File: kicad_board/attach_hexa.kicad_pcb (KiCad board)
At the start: 2 copper layers, 91.3 x 25.9 mm, 26 parts, among them J1 Conn_01x15_Male, J2 TACH, J3 Conn_01x15, J4 Conn_01x15, J5 Conn_01x15_Male, Q1 2N3904, Q2 2N3904, Q3 2N3904, Q4 2N3904, Q5 2N3904, Q6 2N3904

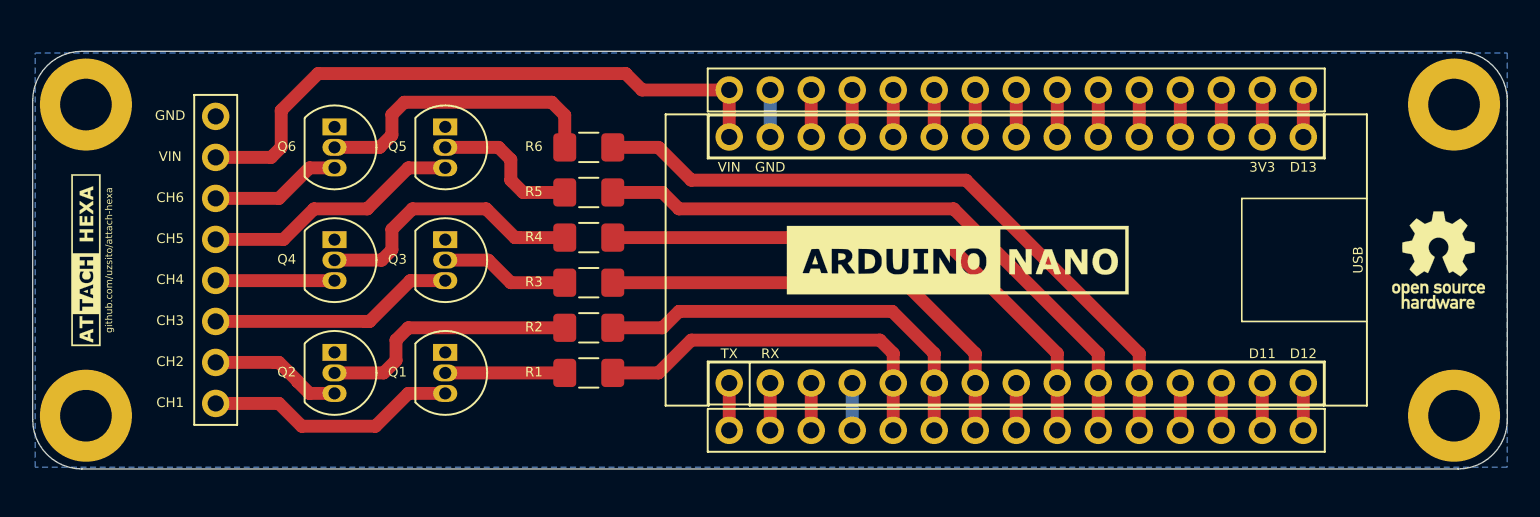
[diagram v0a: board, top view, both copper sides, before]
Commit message: Changed SMD sizes to ease hand soldering. Improved silkscreen visibility.
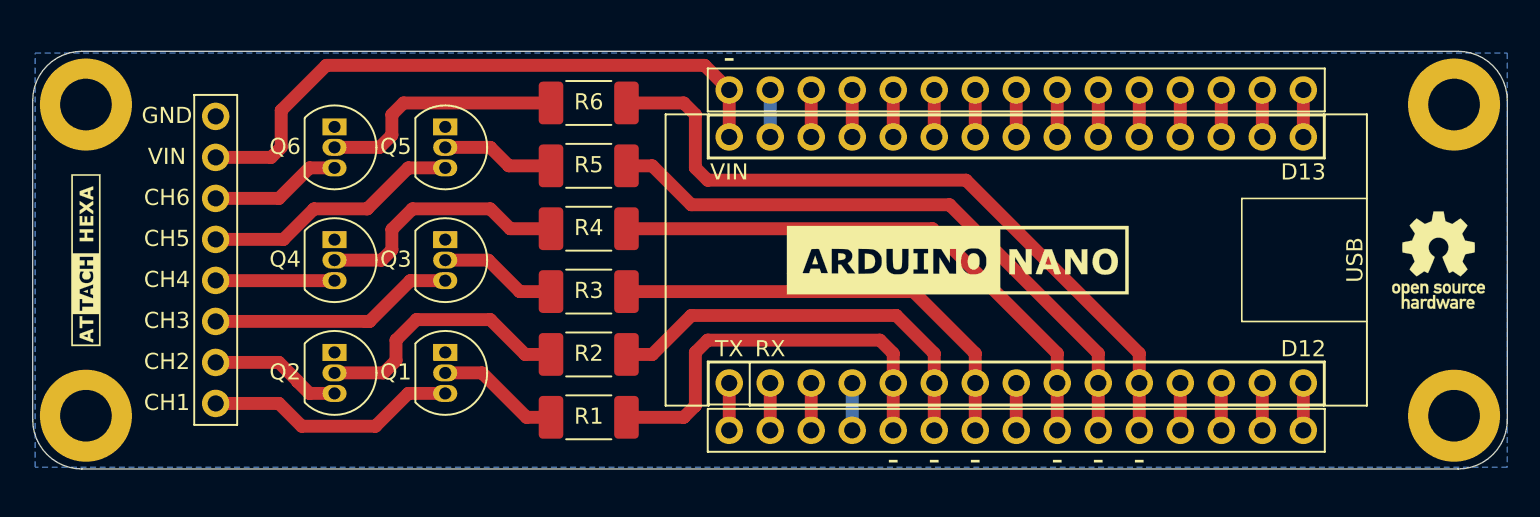
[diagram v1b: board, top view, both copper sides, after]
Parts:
- R1, R2, R3, R4, R5, R6: footprint Resistor_SMD:R_1206_3216Metric_Pad1.42x1.75mm_HandSolder -> Resistor_SMD:R_2010_5025Metric_Pad1.52x2.65mm_HandSolder
- moved R1 2.75 mm to (166.9, 87.8)
- moved R6 2.75 mm to (166.9, 68.4)
- moved R5 1.65 mm to (166.9, 72.3)
- moved R2 1.65 mm to (166.9, 83.9)
- moved R3 0.55 mm to (166.9, 80.1)
- moved R4 0.55 mm to (166.9, 76.2)
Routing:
- net Net-(Q6-Pad2): track 18.5 -> 15.3 mm
- net Net-(Q5-Pad2): track 9.30 -> 7.03 mm
- net Net-(A1-Pad5): track 23.3 -> 25.5 mm
- net Net-(A1-Pad11): track 42.7 -> 44.9 mm
- net Net-(A1-Pad7): track 29.0 -> 28.0 mm
- net Net-(Q4-Pad2): track 17.1 -> 16.0 mm
- net Net-(A1-Pad9): track 35.3 -> 34.6 mm
- net Net-(Q3-Pad2): track 7.98 -> 7.36 mm
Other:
- board text added: "-"
- board text removed: "github.com/uzsito/attach-hexa"

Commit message: Minor trace routing, positioning and silkscreen adjustments
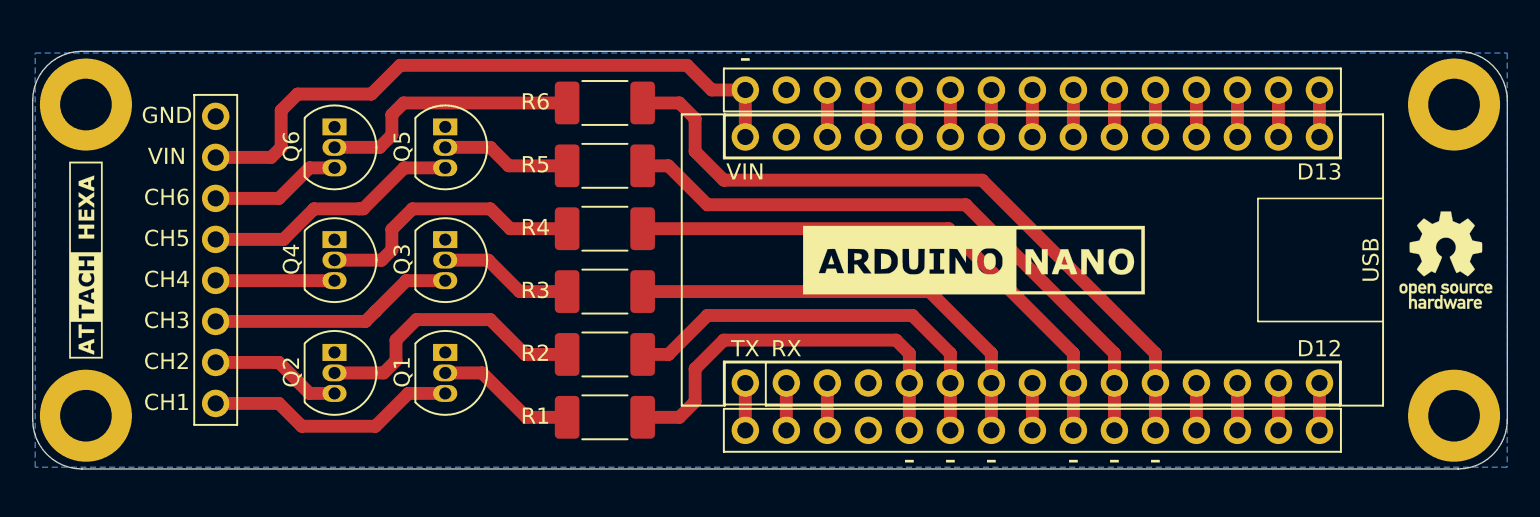
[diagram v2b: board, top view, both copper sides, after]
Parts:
- removed the G*** at (135.7, 78.1)
- added G***: LOGO, Symbol:attach_hexa_logo2, F.Cu at (135.7, 78.1)
- moved A1 1.00 mm to (176.6, 85.7)
- moved G*** 1.00 mm to (190.7, 78.1)
- moved J1 1.00 mm to (212.1, 67.6)
- moved J3 1.00 mm to (212.1, 70.5)
- moved J4 1.00 mm to (176.6, 85.7)
- moved J5 1.00 mm to (176.6, 88.6)
- moved R1 1.00 mm to (167.9, 87.8)
- moved R2 1.00 mm to (167.9, 83.9)
- moved R3 1.00 mm to (167.9, 80.1)
- moved R4 1.00 mm to (167.9, 76.2)
- moved R5 1.00 mm to (167.9, 72.3)
- moved R6 1.00 mm to (167.9, 68.4)
- moved REF** 0.45 mm to (220.0, 78.1)
- moved REF** 0.24 mm to (194.4, 77.3)
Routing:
- net GND: track 5.84 -> 0.00 mm
- net Net-(A1-Pad30): track 38.5 -> 39.5 mm
- net Net-(Q6-Pad2): track 15.3 -> 16.3 mm
- net Net-(Q5-Pad2): track 7.03 -> 8.03 mm
- net Net-(Q4-Pad2): track 16.0 -> 17.0 mm
- net Net-(Q3-Pad2): track 7.36 -> 8.36 mm
- net Net-(Q2-Pad2): track 16.4 -> 17.4 mm
- net Net-(Q1-Pad2): track 7.69 -> 8.69 mm
- net Net-(A1-Pad11): track 44.9 -> 44.1 mm
- net Net-(A1-Pad5): track 25.5 -> 24.8 mm

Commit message: Set base resistors to 4.7k - force transistor saturation up to 10mA collector current
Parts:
- R1, R2, R3, R4, R5, R6: value R -> 4,7k
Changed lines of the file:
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@@
   )
   (setup
-    (last_trace_width 0.8)
+    (last_trace_width 0.25)
     (user_trace_width 0.6)
     (user_trace_width 0.8)
@@
       (effects (font (size 1 1) (thickness 0.15)))
     )
-    (fp_text value R (at 0 2.28) (layer F.Fab)
+    (fp_text value 4,7k (at 0 2.28) (layer F.Fab)
       (effects (font (size 1 1) (thickness 0.15)))
     )
@@
       (effects (font (size 1 1) (thickness 0.15)))
     )
-    (fp_text value R (at 0 2.28) (layer F.Fab)
+    (fp_text value 4,7k (at 0 2.28) (layer F.Fab)
       (effects (font (size 1 1) (thickness 0.15)))
     )
@@
       (effects (font (size 1 1) (thickness 0.15)))
     )
-    (fp_text value R (at 0 2.28) (layer F.Fab)
+    (fp_text value 4,7k (at 0 2.28) (layer F.Fab)
       (effects (font (size 1 1) (thickness 0.15)))
     )
@@
       (effects (font (size 1 1) (thickness 0.15)))
     )
-    (fp_text value R (at 0 2.28) (layer F.Fab)
+    (fp_text value 4,7k (at 0 2.28) (layer F.Fab)
       (effects (font (size 1 1) (thickness 0.15)))
     )
@@
       (effects (font (size 1 1) (thickness 0.15)))
     )
-    (fp_text value R (at 0 2.28) (layer F.Fab)
+    (fp_text value 4,7k (at 0 2.28) (layer F.Fab)
       (effects (font (size 1 1) (thickness 0.15)))
     )
@@
       (effects (font (size 1 1) (thickness 0.15)))
     )
-    (fp_text value R (at 0 2.28) (layer F.Fab)
-      (effects (font (size 1 1) (thickness 0.15)))
-    )
+    (fp_text value 4,7k (at 0 2.28) (layer F.Fab)
+      (effects (font (size 1 1) (thickness 0.15)))
+    )

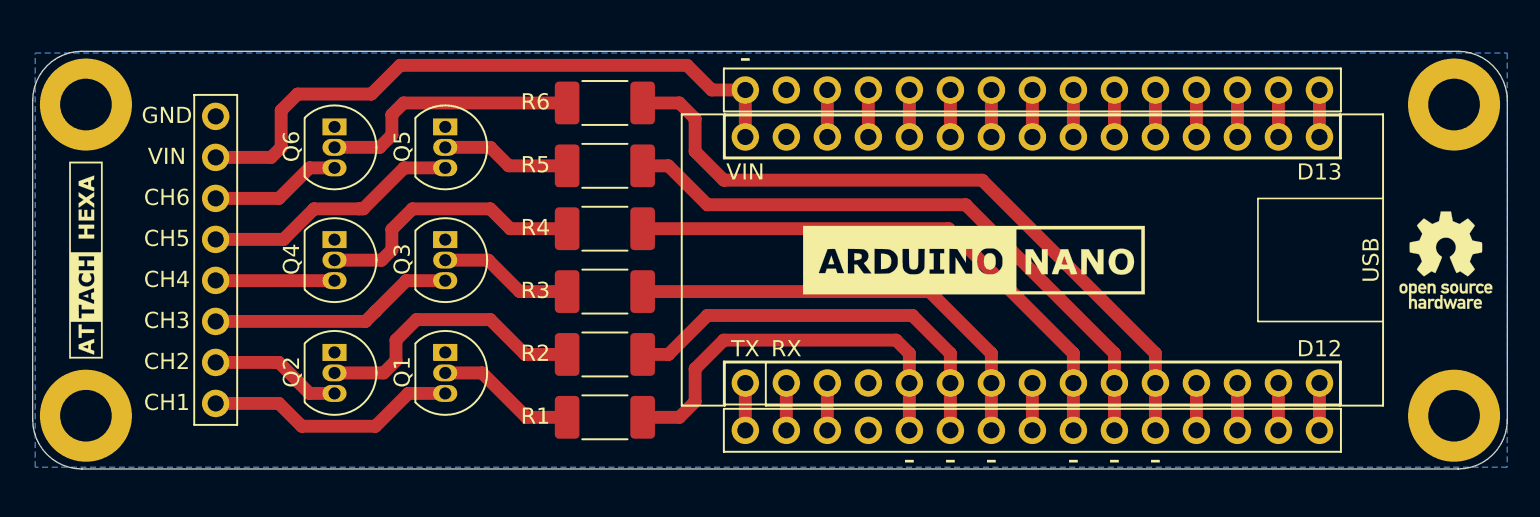
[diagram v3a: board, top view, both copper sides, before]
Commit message: Updated silkscreen
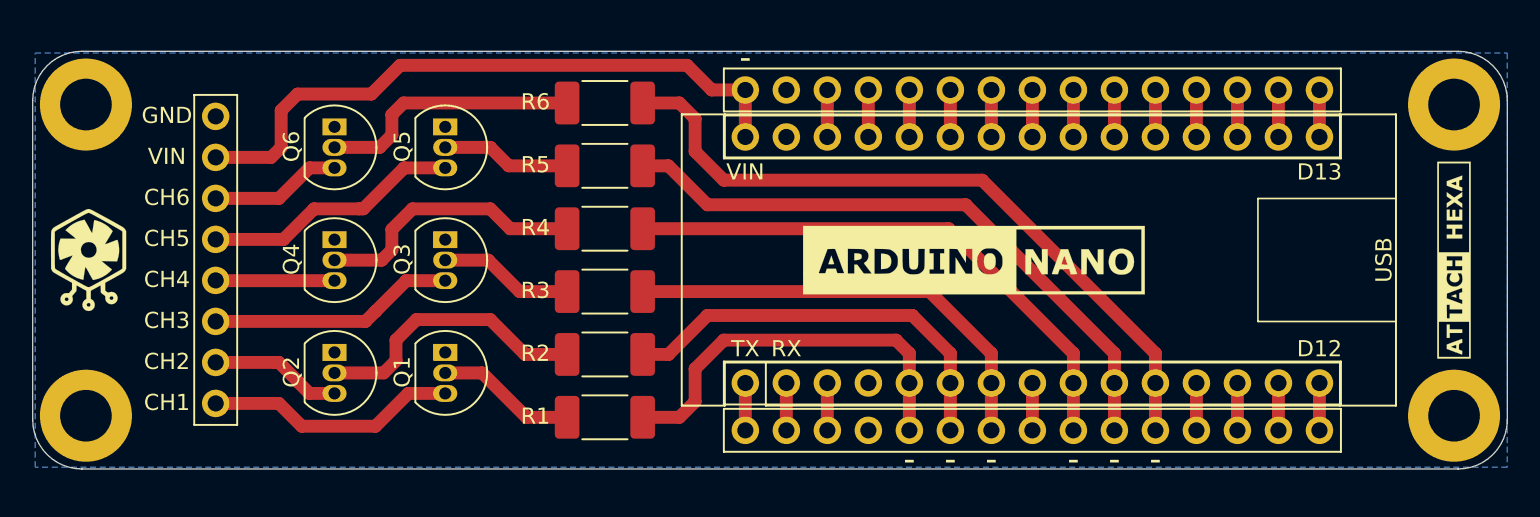
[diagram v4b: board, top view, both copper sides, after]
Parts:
- removed the REF** at (220.0, 78.1)
- added G***: LOGO, Symbol:hexa, F.Cu at (135.9, 78.2)
- moved G*** 84.7 mm to (220.5, 78.1)
